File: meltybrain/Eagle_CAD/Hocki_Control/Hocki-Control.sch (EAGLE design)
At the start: 92 parts, among them U1 TEENSY_4.1, U10 TLV3502AIDCNR, U11 NL27WZ32USG, U12 NL27WZ32USG, U13 HMC1052L-TR, U14 LMV358, U15 IRF7509, U16 TMUX1219DCKR, U17 LMV358, U18 LMV358, U2 ADXL375, U3 ADXL375, U4 ADXL375, U5 ADXL375, U6 LMH6612MAX/NOPB, U7 LMH6612MAX/NOPB, U8 LMH6612MAX/NOPB, U9 LMH6612MAX/NOPB

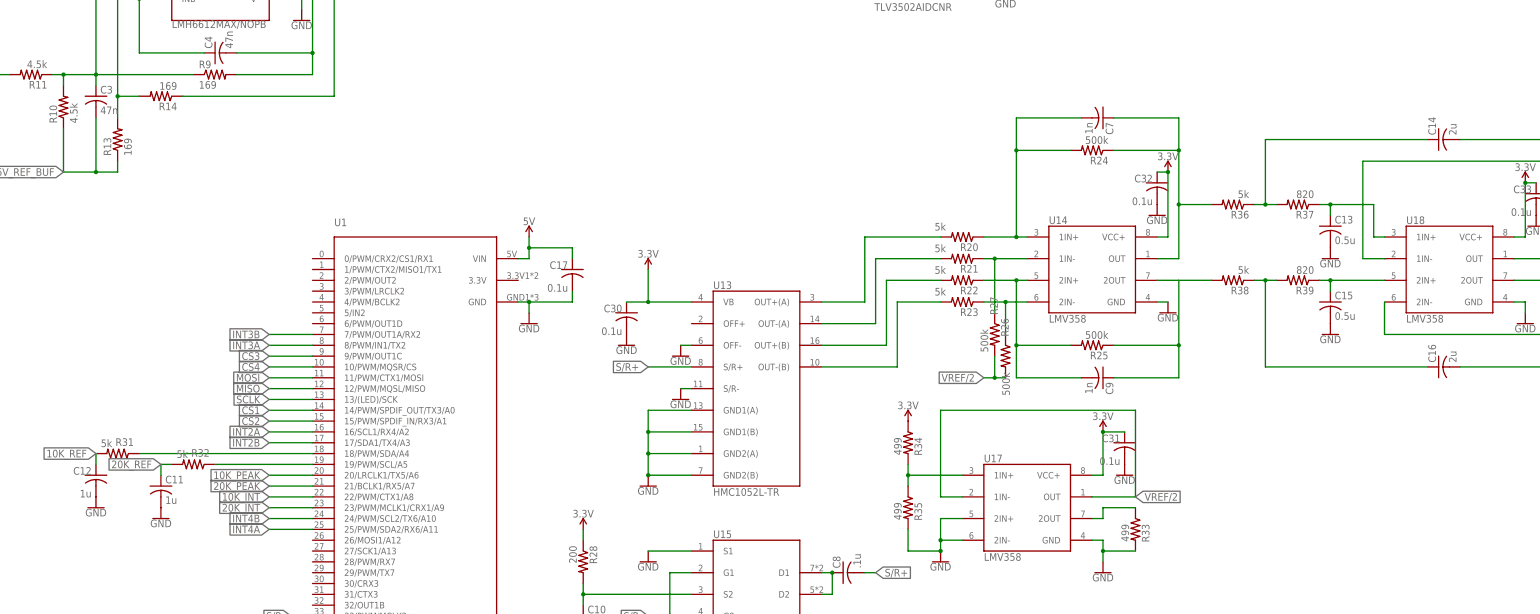
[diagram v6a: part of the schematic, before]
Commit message: done...kinda
control is routed
power stuff is missing
magnetometer keepout was too big...
bom is updated to this point
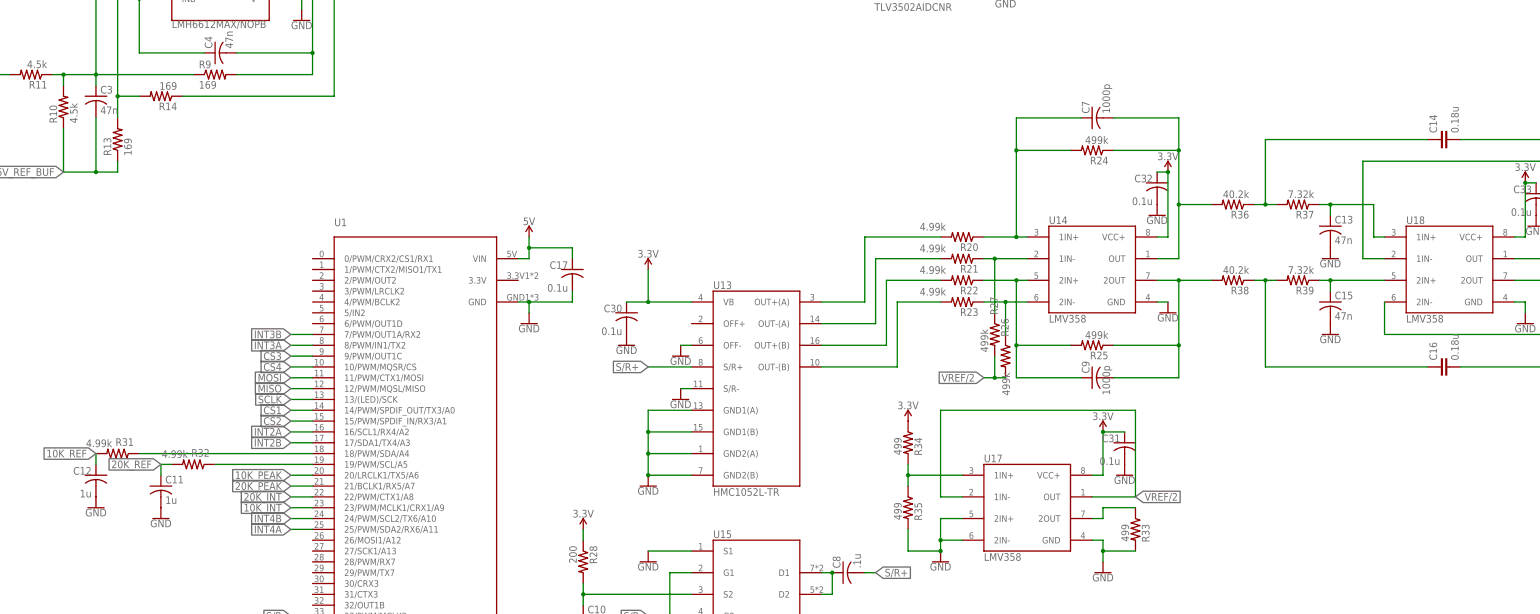
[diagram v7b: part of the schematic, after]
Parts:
- C13, C15: value 0.5u -> 47n; device rcl:C-USC0603 -> rcl:C-USC1206
- C14, C16: value 2u -> 0.18u; device rcl:C-USC0603 -> Hocki_Library:ECH-U1H184GX9
- C7, C9: value 1n -> 1000p; device rcl:C-USC0603 -> rcl:C-USC0805
- R20, R21, R22, R23, R31, R32: value 5k -> 4.99k
- R24, R25, R26, R27: value 500k -> 499k
- R36, R38: value 5k -> 40.2k
- R37, R39: value 820 -> 7.32k
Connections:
- removed net MAG_OUTPUTA1: R38.2
- net 10K_INT: now also U1.23/PWM/MCLK1/CRX1/A9; no longer U1.22/PWM/CTX1/A8
- net 20K_INT: now also U1.22/PWM/CTX1/A8; no longer U1.23/PWM/MCLK1/CRX1/A9
- net MAG_OUTPUTA: now also C7.2; no longer C7.1
- net MAG_OUTPUTB: now also C9.2, R38.2; no longer C9.1
- net N$35: now also C9.1; no longer C9.2
- net N$37: now also C7.1; no longer C7.2
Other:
- moved on the sheet: C7, C9

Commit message: Added jst-sr connector and edited text labels
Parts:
- added J1: JST-SR_5, Hocki_Library:JST-SR_5
- added P1, P2: B5B-PH-K, con-jst-ph:B5B-PH-K
- added P3: B2B-PH-K, con-jst-ph:B2B-PH-K
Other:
- moved on the sheet: C1, C10, C11, C12, C13, C14, C15, C16, C17, C18, C19, C2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
